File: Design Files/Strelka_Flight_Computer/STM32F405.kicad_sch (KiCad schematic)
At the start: 23 parts, among them SW1 SW_Push, SW2 SW_Push, U5 STM32F405RGTx, Y1 Q13FC1350000200, Y2 X322524MOB4SI

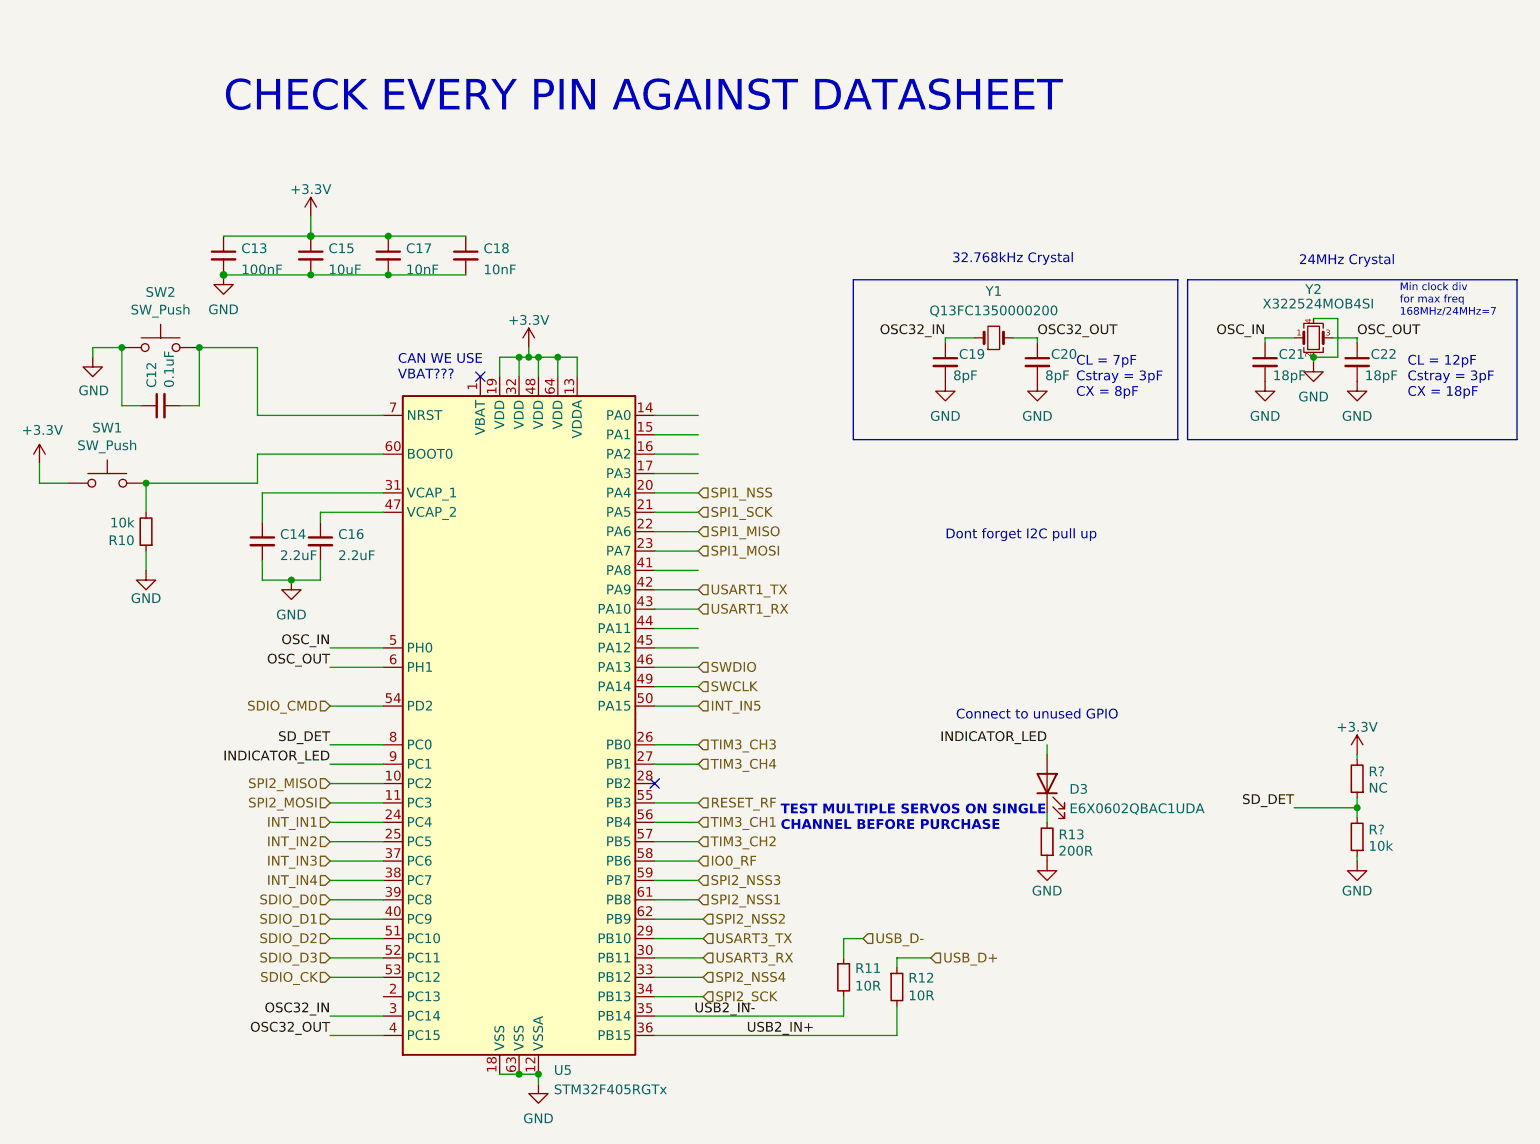
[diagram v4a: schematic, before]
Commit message: Added motor driver to power board
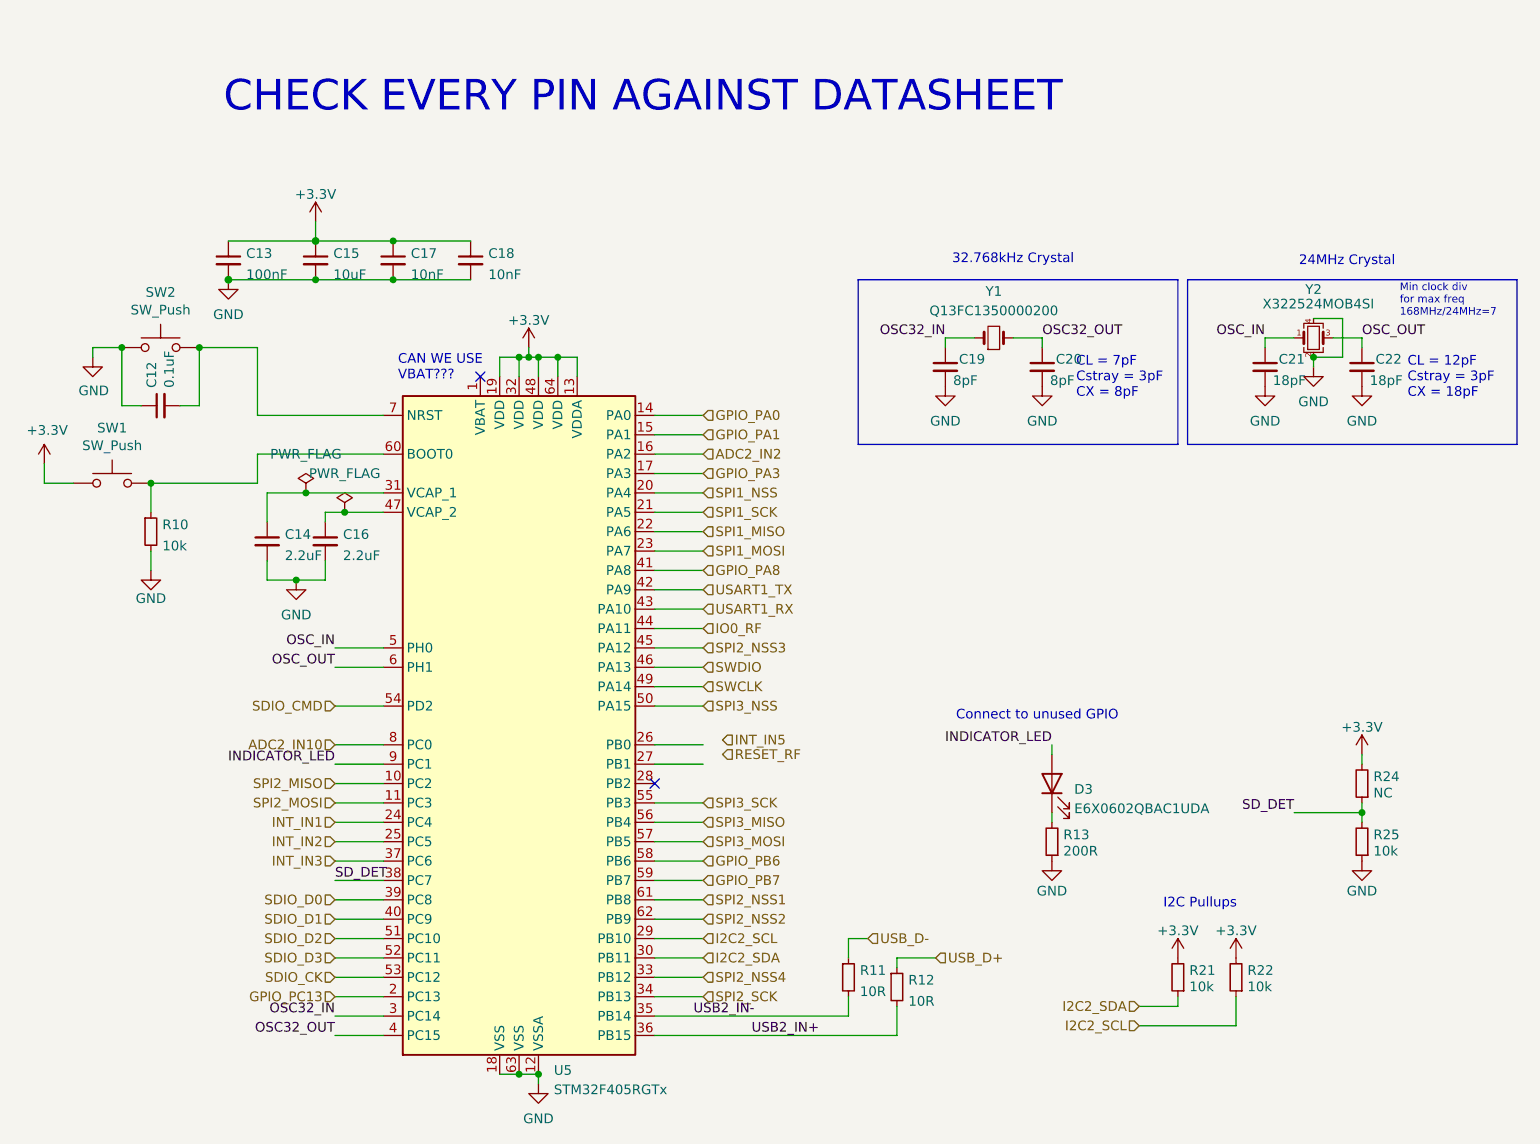
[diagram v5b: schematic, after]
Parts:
- removed R10: 10k, Resistor_SMD:R_0603_1608Metric_Pad0.98x0.95mm_HandSolder, symbol Nebula-rescue:R_Small-Device-H7_FlightComputer-rescue
- removed R11, R12: 10R, Resistor_SMD:R_0603_1608Metric_Pad0.98x0.95mm_HandSolder, symbol Nebula-rescue:R_Small-Device-H7_FlightComputer-rescue
- added R10: 10k, Resistor_SMD:R_0603_1608Metric, symbol Device:R_Small
- added R11, R12: 10R, Resistor_SMD:R_0603_1608Metric, symbol Device:R_Small
- added R21, R22: 10k, Resistor_SMD:R_0603_1608Metric_Pad0.98x0.95mm_HandSolder, symbol Device:R_Small
- gave numbers to parts that had none: 2
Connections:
- net INT_IN4 is gone; now on net SD_DET: U5.38 (PC7)
- net +3V3: now also R21.2, R22.2
- net GND: now also R10.2
- net INT_IN5: no longer U5.50 (PA15)
- net IO0_RF: now also U5.44 (PA11); no longer U5.58 (PB6)
- net RESET_RF: no longer U5.55 (PB3)
- net SD_DET: no longer U5.8 (PC0)
- net SPI2_NSS3: now also U5.45 (PA12); no longer U5.59 (PB7)
- net USB2_IN+: now also R12.2
- net USB2_IN-: now also R11.2
- net USB_D+: now also R12.1
- net USB_D-: now also R11.1
- net at SW1.2, U5.60 (BOOT0): now also R10.1
- net GPIO_PA0: now reaches U5.14 (PA0)
- net GPIO_PA1: now reaches U5.15 (PA1)
- net ADC2_IN2: now reaches U5.16 (PA2)
- net GPIO_PA3: now reaches U5.17 (PA3)
- net GPIO_PC13: now reaches U5.2 (PC13)
- net GPIO_PA8: now reaches U5.41 (PA8)
- net TIM3_CH1 renamed SPI3_MISO
- net TIM3_CH2 renamed SPI3_MOSI
- net TIM3_CH3: no longer names the net of U5.26 (PB0)
- net TIM3_CH4: no longer names the net of U5.27 (PB1)
- net USART3_RX renamed I2C2_SDA
- net I2C2_SDA: now also R21.1
- net USART3_TX renamed I2C2_SCL
- net I2C2_SCL: now also R22.1
- new net ADC2_IN10: U5.8 (PC0)
- new net GPIO_PB6: U5.58 (PB6)
- new net GPIO_PB7: U5.59 (PB7)
- new net SPI3_NSS: U5.50 (PA15)
- new net SPI3_SCK: U5.55 (PB3)
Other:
- note added: "I2C Pullups"
- note removed: "Dont forget I2C pull up"
- note removed: "TEST MULTIPLE SERVOS ON SINGLE CHANNEL BEFORE PURCHASE"
- moved on the sheet: C13, C14, C15, C16, C17, C18, C19, C20, C21, C22, D3, R13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

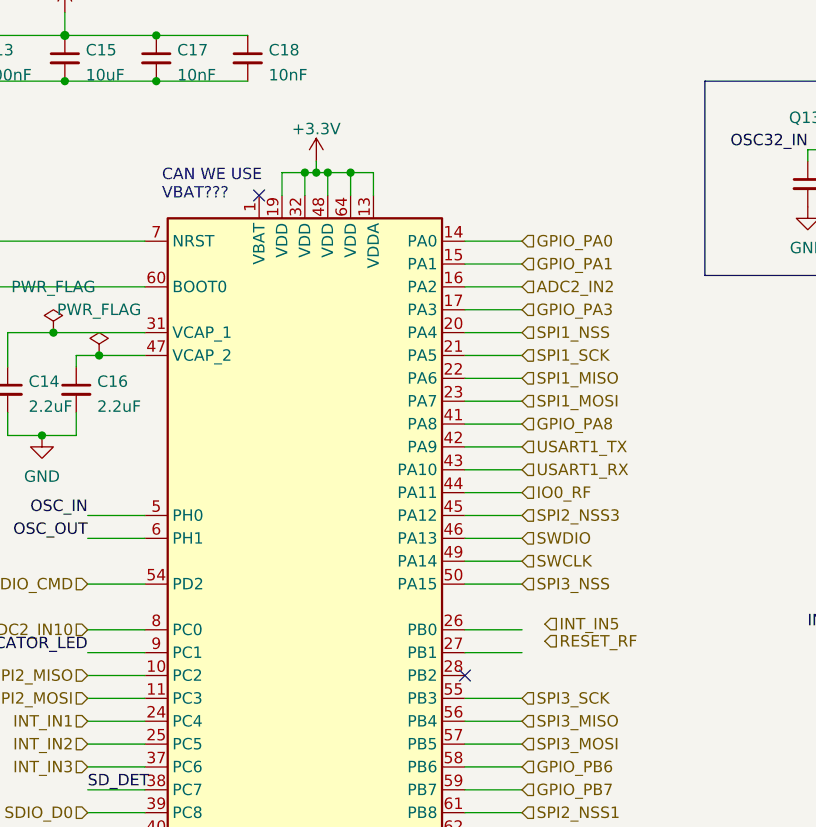
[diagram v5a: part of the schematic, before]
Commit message: Changed boost converter
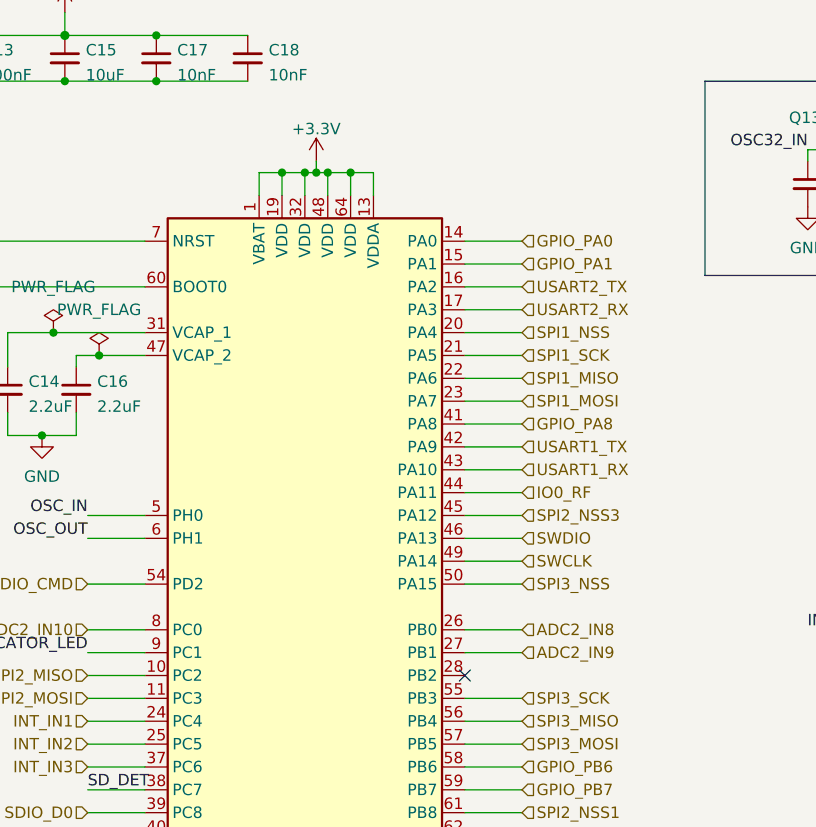
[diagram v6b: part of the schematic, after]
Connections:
- net +3V3: now also U5.1 (VBAT)
- net ADC2_IN8: now reaches U5.26 (PB0)
- net ADC2_IN9: now reaches U5.27 (PB1)
- net ADC2_IN2 renamed USART2_TX
- net GPIO_PA3 renamed USART2_RX
- no-connect marks 2 -> 1
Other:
- note removed: "CAN WE USE VBAT???"
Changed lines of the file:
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@@
   (junction (at 119.38 44.45) (diameter 0) (color 0 0 0 0)
   )
+  (junction (at 133.35 59.69) (diameter 0) (color 0 0 0 0)
+  )
   (junction (at 135.89 153.67) (diameter 0) (color 0 0 0 0)
   )
@@
   (junction (at 138.43 59.69) (diameter 0) (color 0 0 0 0)
   )
-  (no_connect (at 130.81 62.23))
   (no_connect (at 153.67 115.57))
   (wire (pts (xy 153.67 80.01) (xy 160.02 80.01))
@@
     (stroke (width 0) (type default) (color 0 0 0 0))
   )
+  (wire (pts (xy 130.81 62.23) (xy 130.81 59.69))
+    (stroke (width 0) (type default) (color 0 0 0 0))
+  )
   (wire (pts (xy 111.76 97.79) (xy 118.11 97.79))
     (stroke (width 0) (type default) (color 0 0 0 0))
@@
     (stroke (width 0) (type default) (color 0 0 0 0))
   )
+  (wire (pts (xy 130.81 59.69) (xy 133.35 59.69))
+    (stroke (width 0) (type default) (color 0 0 0 0))
+  )
   (wire (pts (xy 138.43 153.67) (xy 138.43 154.94))
     (stroke (width 0) (type default) (color 0 0 0 0))
@@
     (effects (font (size 1.27 1.27)) (justify left bottom))
   )
-  (text "CAN WE USE \nVBAT???" (at 120.015 62.865 0)
-    (effects (font (size 1.27 1.27)) (justify left bottom))
-  )
   (text "CHECK EVERY PIN AGAINST DATASHEET" (at 97.155 27.94 0)
     (effects (font (size 4 4)) (justify left bottom))
@@
     (effects (font (size 1.27 1.27)) (justify left))
   )
-  (hierarchical_label "INT_IN5" (shape input) (at 162.56 109.855 0)
+  (hierarchical_label "ADC2_IN8" (shape input) (at 160.02 110.49 0)
     (effects (font (size 1.27 1.27)) (justify left))
   )
@@
     (effects (font (size 1.27 1.27)) (justify left))
   )
-  (hierarchical_label "RESET_RF" (shape input) (at 162.56 111.76 0)
+  (hierarchical_label "ADC2_IN9" (shape input) (at 160.02 113.03 0)
     (effects (font (size 1.27 1.27)) (justify left))
   )
@@
     (effects (font (size 1.27 1.27)) (justify left))
   )
-  (hierarchical_label "GPIO_PA3" (shape input) (at 160.02 74.93 0)
-    (effects (font (size 1.27 1.27)) (justify left))
-  )
-  (hierarchical_label "ADC2_IN2" (shape input) (at 160.02 72.39 0)
-    (effects (font (size 1.27 1.27)) (justify left))
-  )
+  (hierarchical_label "USART2_RX" (shape input) (at 160.02 74.93 0)
+    (effects (font (size 1.27 1.27)) (justify left))
+  )
+  (hierarchical_label "USART2_TX" (shape input) (at 160.02 72.39 0)
+    (effects (font (size 1.27 1.27)) (justify left))
+  )

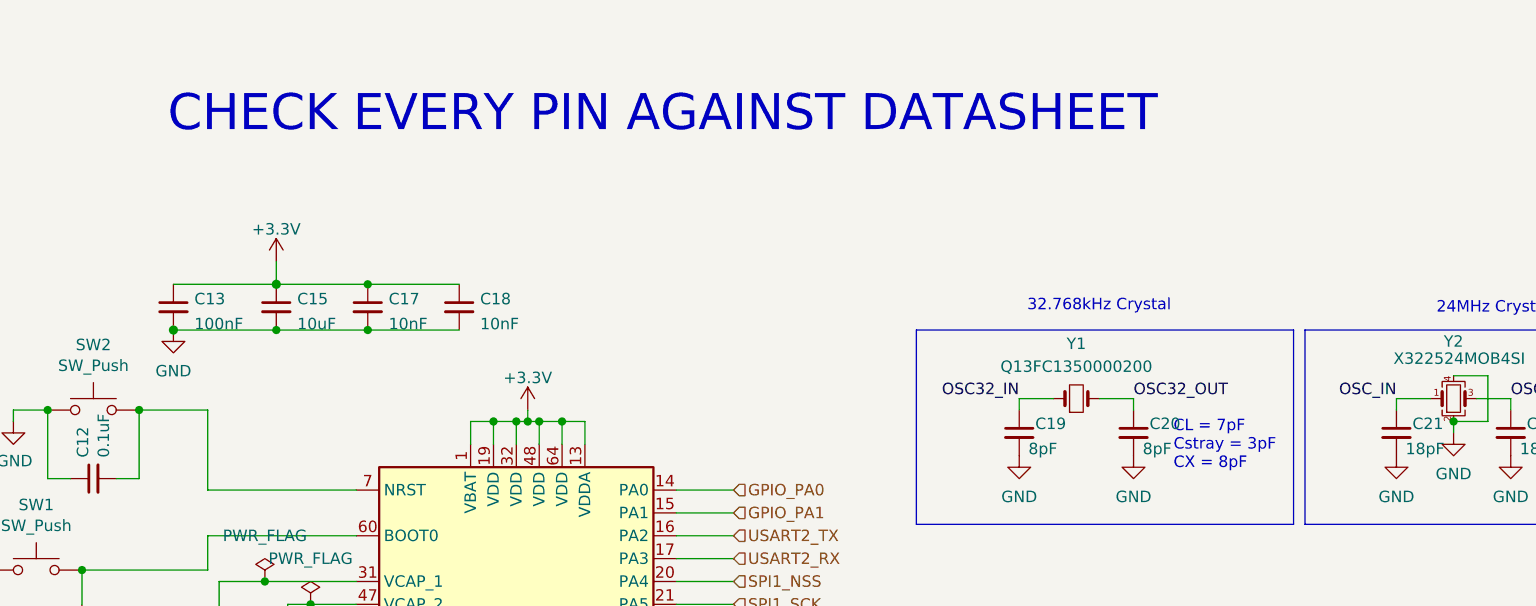
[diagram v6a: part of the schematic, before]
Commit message: Started component placement
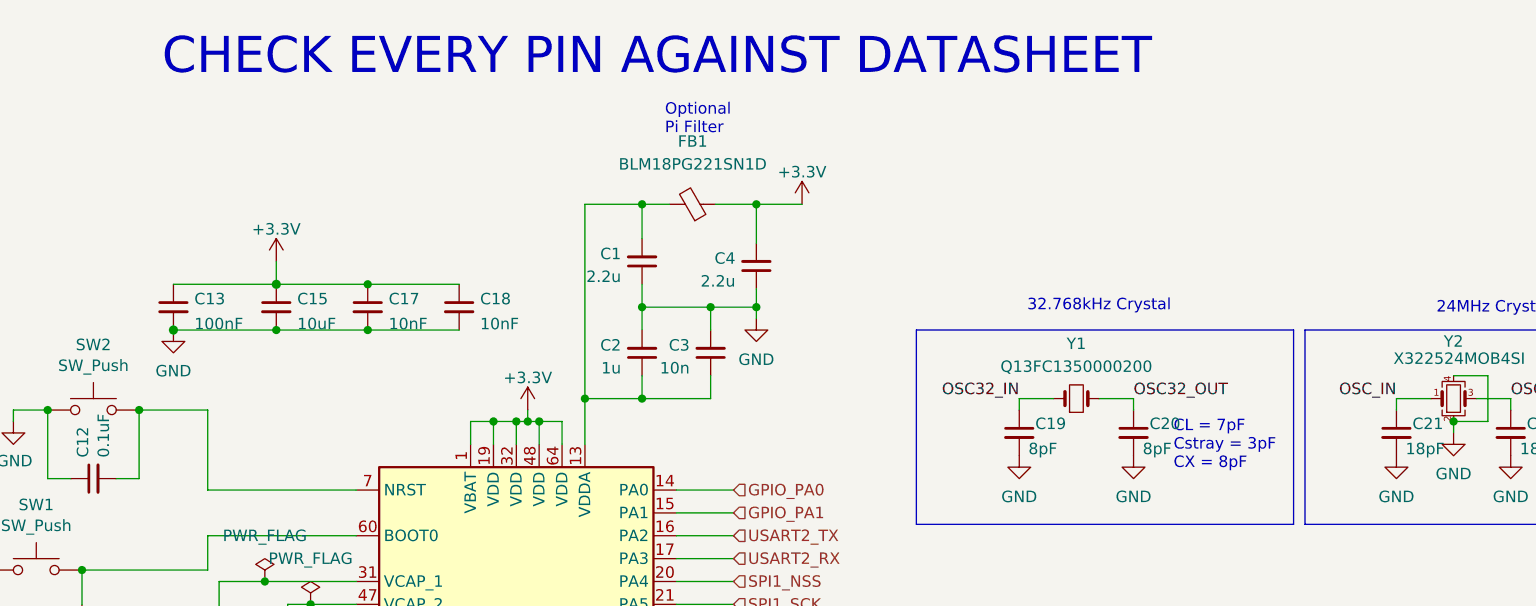
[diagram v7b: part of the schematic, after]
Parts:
- added C1, C4: 2.2u, Capacitor_SMD:C_0603_1608Metric, symbol Device:C_Small
- added C2: 1u, Capacitor_SMD:C_0603_1608Metric, symbol Device:C_Small
- added C3: 10n, Capacitor_SMD:C_0603_1608Metric, symbol Device:C_Small
- added FB1: BLM18PG221SN1D, Inductor_SMD:L_0603_1608Metric, symbol Device:FerriteBead_Small
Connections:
- net +3V3: now also C4.2, FB1.1; no longer U5.13 (VDDA)
- net GND: now also C1.1, C2.2, C3.2, C4.1
- new net: C1.2, C2.1, C3.1, FB1.2, U5.13 (VDDA)
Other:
- note added: "Optional Pi Filter"

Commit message: Creating BOM
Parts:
- D3: MFR# E6X0602QBAC1UDA -> (none)
- U5: LCSC# (none) -> C15742
- Y1: LCSC C48615 -> (none); LCSC# (none) -> C48615
- Y2: LCSC C70590 -> (none); LCSC# (none) -> C70590
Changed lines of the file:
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@@
       (effects (font (size 1.27 1.27)) hide)
     )
-    (property "LCSC" "C48615" (id 4) (at 198.12 57.15 0)
+    (property "LCSC#" "C48615" (id 4) (at 198.12 57.15 0)
       (effects (font (size 1.27 1.27)) hide)
     )
@@
     )
     (property "LCSC#" "C375467" (id 4) (at 205.74 115.57 90)
-      (effects (font (size 1.27 1.27)) hide)
-    )
-    (property "MFR#" "E6X0602QBAC1UDA" (id 5) (at 205.74 115.57 90)
       (effects (font (size 1.27 1.27)) hide)
     )
@@
     )
     (property "Datasheet" "http://www.st.com/st-web-ui/static/active/en/resource/technical/document/datasheet/DM00037051.pdf" (id 3) (at 135.89 107.95 0)
+      (effects (font (size 1.27 1.27)) hide)
+    )
+    (property "LCSC#" "C15742" (id 4) (at 135.89 107.95 0)
       (effects (font (size 1.27 1.27)) hide)
     )
@@
       (effects (font (size 1.27 1.27)) hide)
     )
-    (property "LCSC" "C70590" (id 4) (at 240.03 57.15 0)
-      (effects (font (size 1.27 1.27)) hide)
-    )
+    (property "LCSC#" "C70590" (id 4) (at 240.03 57.15 0)
+      (effects (font (size 1.27 1.27)) hide)
+    )
